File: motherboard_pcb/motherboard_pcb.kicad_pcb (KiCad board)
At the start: 2 copper layers, 27 parts, among them J1 12 Power Supply Input, J6 OLED Display I2C, U1 ESP32-DEVKIT-V1

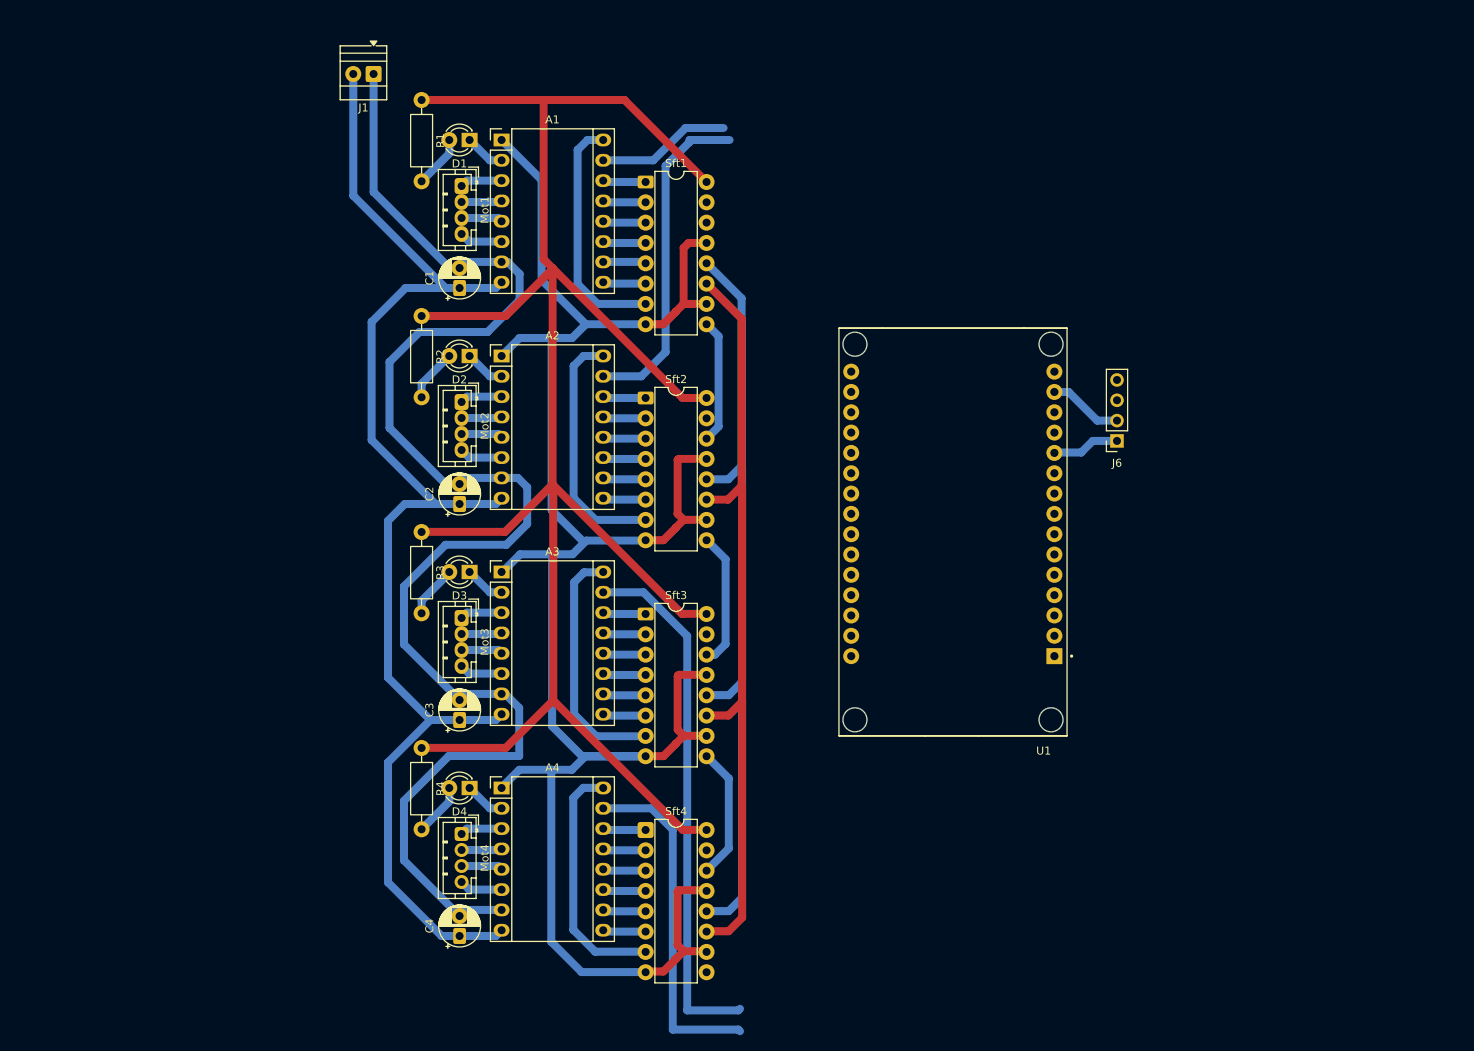
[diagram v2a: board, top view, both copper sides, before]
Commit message: Routed all connections to shift registers
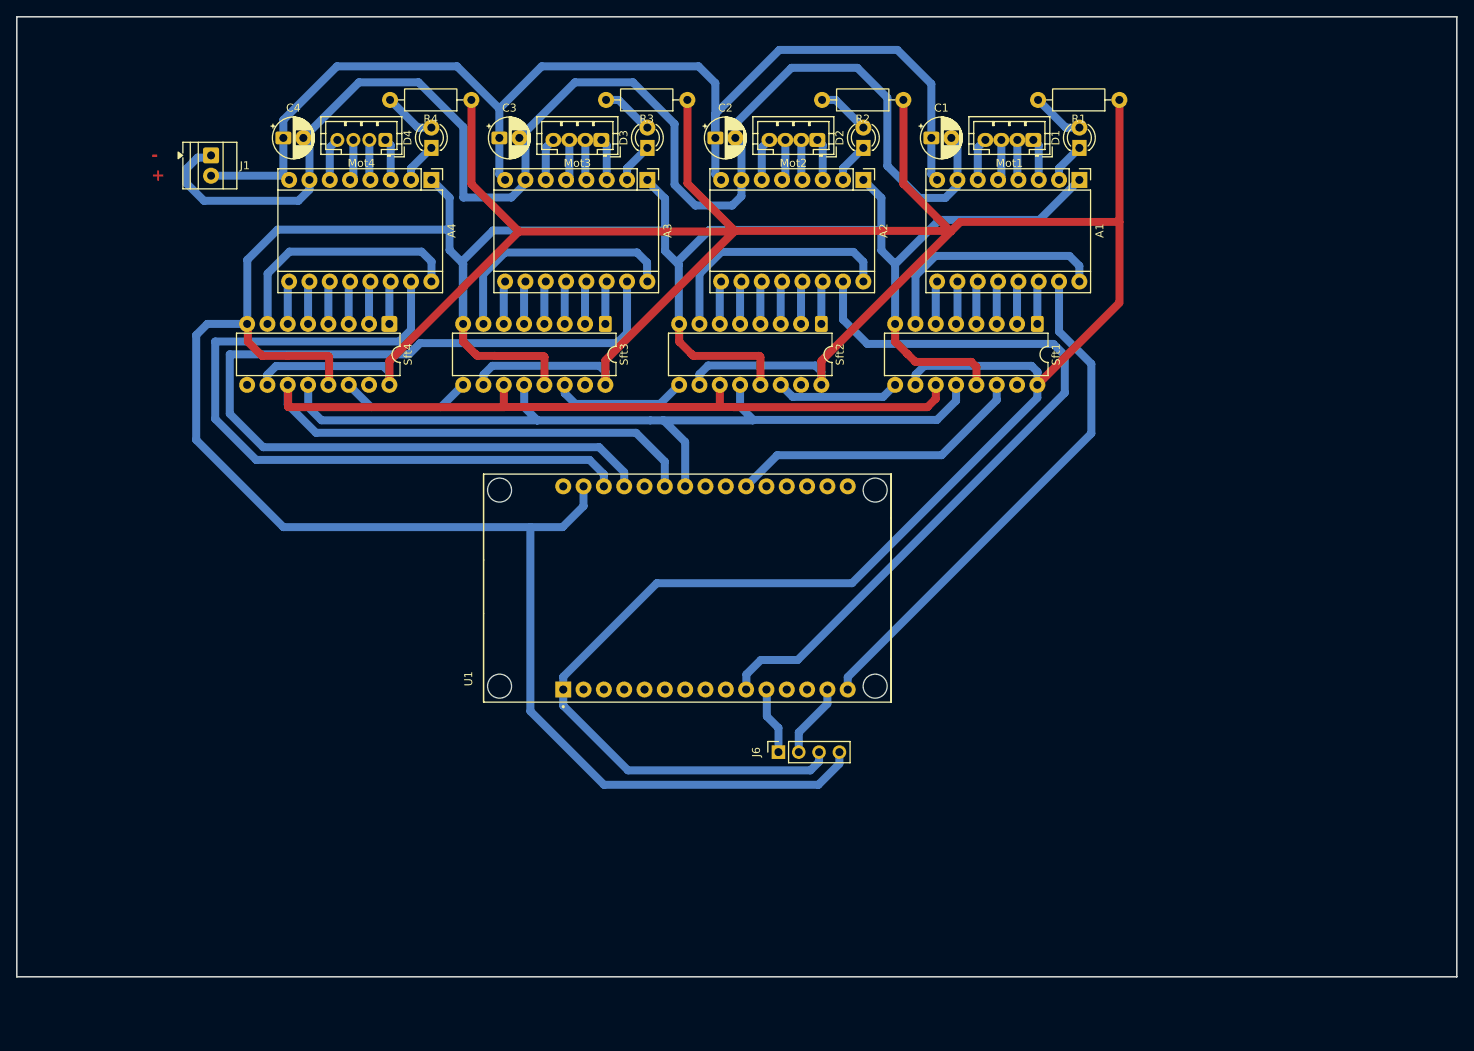
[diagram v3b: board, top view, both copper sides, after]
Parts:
- moved C4 102.2 mm to (72.7, 49.7), turned to 0 degrees
- moved Mot4 87.3 mm to (85.5, 50.0), turned to 180 degrees
- moved R1 87.2 mm to (177.2, 45.0), turned to 180 degrees
- moved R4 81.2 mm to (96.2, 45.0), turned to 180 degrees
- moved D4 80.2 mm to (91.2, 51.0), turned to 90 degrees
- moved A4 76.5 mm to (91.2, 55.0), turned to -90 degrees
- moved D1 76.2 mm to (172.2, 51.0), turned to 90 degrees
- moved C3 72.9 mm to (99.7, 49.7), turned to 0 degrees
- moved A1 72.4 mm to (172.2, 55.0), turned to -90 degrees
- moved Mot1 71.7 mm to (166.5, 50.0), turned to 180 degrees
- moved Sft4 70.9 mm to (86.0, 73.0), turned to -90 degrees
- moved R2 66.0 mm to (150.2, 45.0), turned to 180 degrees
- moved R3 63.4 mm to (123.2, 45.0), turned to 180 degrees
- moved Mot3 62.3 mm to (112.5, 50.0), turned to 180 degrees
- moved C1 61.9 mm to (153.7, 49.7), turned to 0 degrees
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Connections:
- Sft1 pad 10: GND -> +3.3V
- Sft2 pad 10: GND -> +3.3V
- Sft3 pad 10: GND -> +3.3V
- Sft4 pad 10: GND -> +3.3V
- U1 pad 10: unconnected-(U1-D19-Pad10) -> STP2
- U1 pad 15: unconnected-(U1-D23-Pad15) -> STP1
- U1 pad 2: GND -> unconnected-(U1-GND-Pad2)
- U1 pad 21: unconnected-(U1-D32-Pad21) -> SER
- U1 pad 24: unconnected-(U1-D26-Pad24) -> RCLK
- U1 pad 25: RCLK -> SRCLK
- U1 pad 26: SRCLR -> unconnected-(U1-D14-Pad26)
- U1 pad 27: SRCLK -> STP3
- U1 pad 28: OE -> STP4
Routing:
- net +3.3V: track 249.8 -> 441.7 mm
- net GND: track 262.2 -> 393.4 mm
- net STP2: track 41.8 -> 95.3 mm
- net STP3: track 66.2 -> 118.7 mm
- net SRCLK: track 96.4 -> 146.9 mm
- net STP4: track 43.3 -> 93.8 mm
- net STP1: track 16.7 -> 65.3 mm
- net SER: track 0.00 -> 37.7 mm
- net +12V: track 172.1 -> 148.8 mm
- net RCLK: track 96.4 -> 107.0 mm
- net -12V: track 184.1 -> 178.3 mm
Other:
- board outline added: 180 x 120 mm
- board text added: "+ -"
